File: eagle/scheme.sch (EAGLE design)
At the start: 9 parts, among them IC1 L293D

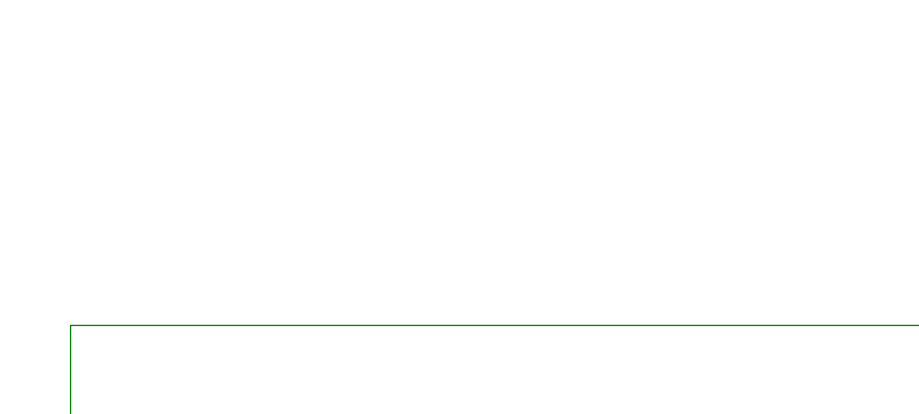
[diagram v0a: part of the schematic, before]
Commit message: Added connection description to scheme
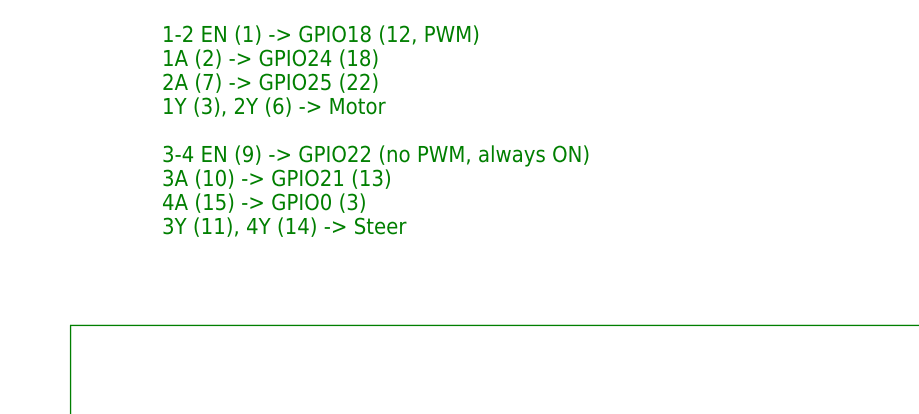
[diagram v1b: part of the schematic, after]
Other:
- note added: "1-2 EN (1) -> GPIO18 (12, PWM) 1A (2) -> GPIO24 (18) 2A (7) -> GPIO25 (22) 1Y (3), 2Y (6) -> Motor 3-4 EN (9) -> GPIO22 (no PWM, always ON) 3A (10) -> GPIO21 (13) 4A (15) -> GPIO0 (3) 3Y (11), 4Y (14) -> Steer"
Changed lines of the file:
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@@
 <circle x="33.02" y="71.12" radius="3.5921" width="0.1524" layer="91"/>
 <text x="30.48" y="71.12" size="1.778" layer="91">Steer</text>
+<text x="0" y="114.3" size="1.778" layer="91">1-2 EN (1) -&gt; GPIO18 (12, PWM)
+1A (2) -&gt; GPIO24 (18)
+2A (7) -&gt; GPIO25 (22)
+1Y (3), 2Y (6) -&gt; Motor
+3-4 EN (9) -&gt; GPIO22 (no PWM, always ON)
+3A (10) -&gt; GPIO21 (13)
+4A (15) -&gt; GPIO0 (3)
+3Y (11), 4Y (14) -&gt; Steer</text>
 </plain>
 <instances>
@@
 </schematic>
 </drawing>
+<compatibility>
+<note version="6.3" minversion="6.2.2" severity="warning">
+Since Version 6.2.2 text objects can contain more than one line,
+which will not be processed correctly with this version.
+</note>
+</compatibility>
 </eagle>

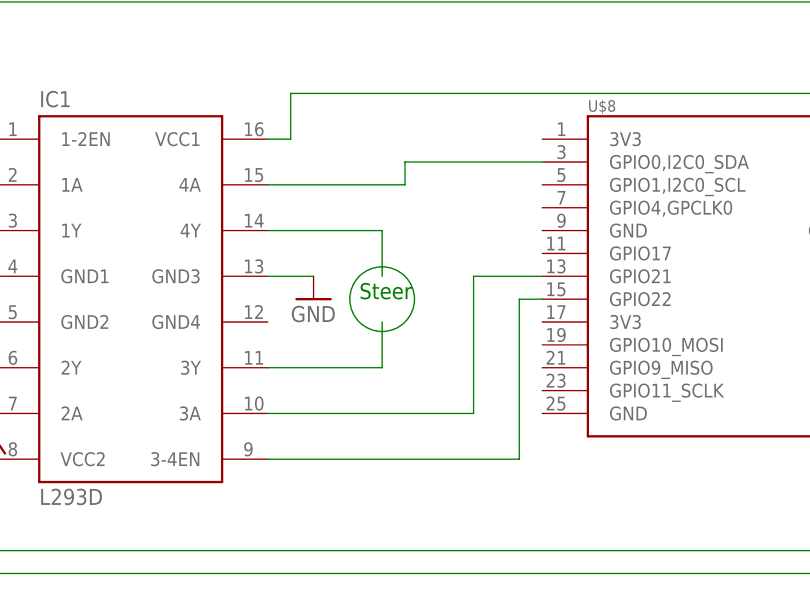
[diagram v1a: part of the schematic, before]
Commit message: Added full control example. Issues with steering power absorbtion
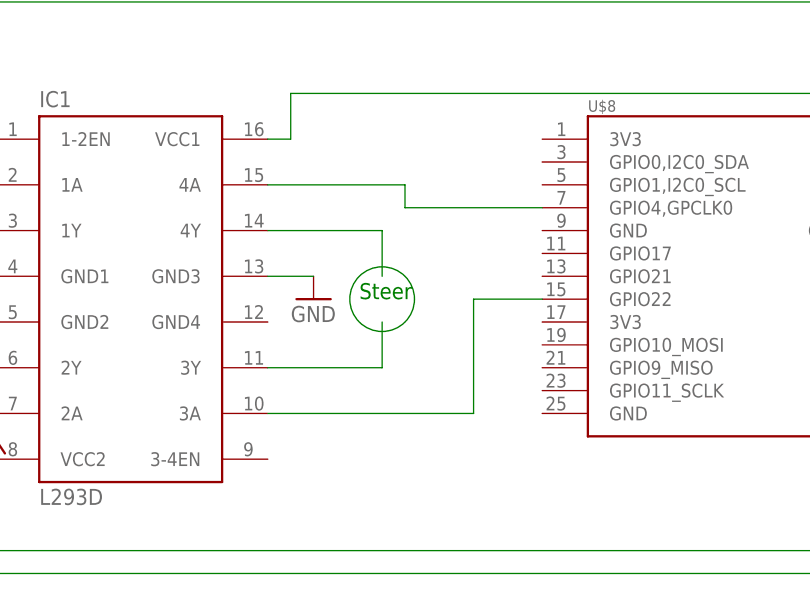
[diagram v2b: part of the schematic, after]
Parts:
- removed U$1, U$2, U$3, U$4, U$5, U$6, U$7: RASPBERRY-PI, RaspberryPi:RASPBERRY-PI
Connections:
- removed net N$6: IC1.3-4EN, U$8.GPIO22
- net N$12: now also U$8.GPIO22
- net N$5: now also U$8.GPIO4,GPCLK0; no longer U$8.GPIO0,I2C0_SDA
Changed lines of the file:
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@@
 <attribute name="MPN" value="L293DNEE4"/>
 </part>
-<part name="U$1" library="RaspberryPi" deviceset="RASPBERRY-PI" device=""/>
-<part name="U$2" library="RaspberryPi" deviceset="RASPBERRY-PI" device=""/>
-<part name="U$3" library="RaspberryPi" deviceset="RASPBERRY-PI" device=""/>
-<part name="U$4" library="RaspberryPi" deviceset="RASPBERRY-PI" device=""/>
-<part name="U$5" library="RaspberryPi" deviceset="RASPBERRY-PI" device=""/>
-<part name="U$6" library="RaspberryPi" deviceset="RASPBERRY-PI" device=""/>
-<part name="U$7" library="RaspberryPi" deviceset="RASPBERRY-PI" device=""/>
 <part name="U$8" library="RaspberryPi" deviceset="RASPBERRY-PI_REV1" device="">
 <attribute name="MF" value=""/>
@@
 <pinref part="IC1" gate="G$1" pin="4A"/>
 <wire x1="20.32" y1="83.82" x2="35.56" y2="83.82" width="0.1524" layer="91"/>
-<wire x1="35.56" y1="83.82" x2="35.56" y2="86.36" width="0.1524" layer="91"/>
-<pinref part="U$8" gate="G$1" pin="GPIO0,I2C0_SDA"/>
-<wire x1="35.56" y1="86.36" x2="50.8" y2="86.36" width="0.1524" layer="91"/>
-</segment>
-</net>
-<net name="N$6" class="0">
-<segment>
-<pinref part="U$8" gate="G$1" pin="GPIO22"/>
-<pinref part="IC1" gate="G$1" pin="3-4EN"/>
-<wire x1="20.32" y1="53.34" x2="48.26" y2="53.34" width="0.1524" layer="91"/>
-<wire x1="48.26" y1="53.34" x2="48.26" y2="71.12" width="0.1524" layer="91"/>
-<wire x1="48.26" y1="71.12" x2="50.8" y2="71.12" width="0.1524" layer="91"/>
+<wire x1="35.56" y1="83.82" x2="35.56" y2="81.28" width="0.1524" layer="91"/>
+<pinref part="U$8" gate="G$1" pin="GPIO4,GPCLK0"/>
+<wire x1="35.56" y1="81.28" x2="50.8" y2="81.28" width="0.1524" layer="91"/>
 </segment>
 </net>
@@
 <net name="N$12" class="0">
 <segment>
-<wire x1="43.18" y1="73.66" x2="50.8" y2="73.66" width="0.1524" layer="91"/>
-<wire x1="43.18" y1="58.42" x2="43.18" y2="73.66" width="0.1524" layer="91"/>
 <pinref part="IC1" gate="G$1" pin="3A"/>
 <wire x1="20.32" y1="58.42" x2="43.18" y2="58.42" width="0.1524" layer="91"/>
+<wire x1="43.18" y1="58.42" x2="43.18" y2="71.12" width="0.1524" layer="91"/>
+<pinref part="U$8" gate="G$1" pin="GPIO22"/>
+<wire x1="43.18" y1="71.12" x2="50.8" y2="71.12" width="0.1524" layer="91"/>
 </segment>
 </net>
